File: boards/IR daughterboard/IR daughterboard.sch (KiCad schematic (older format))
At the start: 1 part, among them P0 HEADER

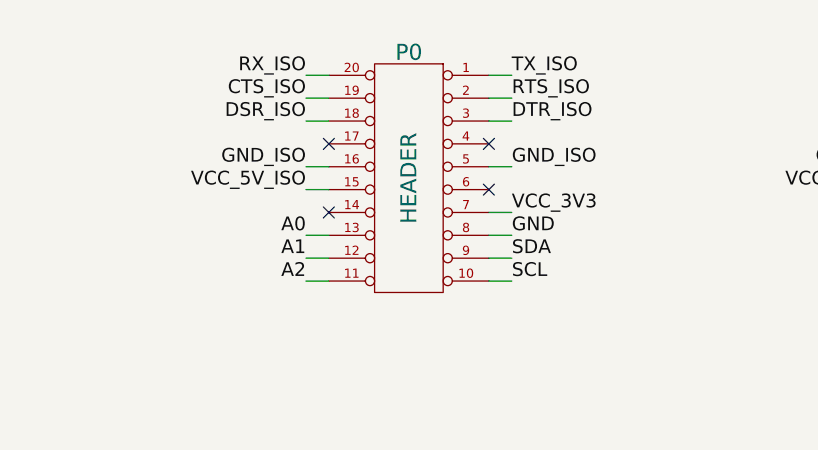
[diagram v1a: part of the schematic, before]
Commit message: Updated daughterboard header pinout in all sheets to be PMOD UART 4/4A compatible
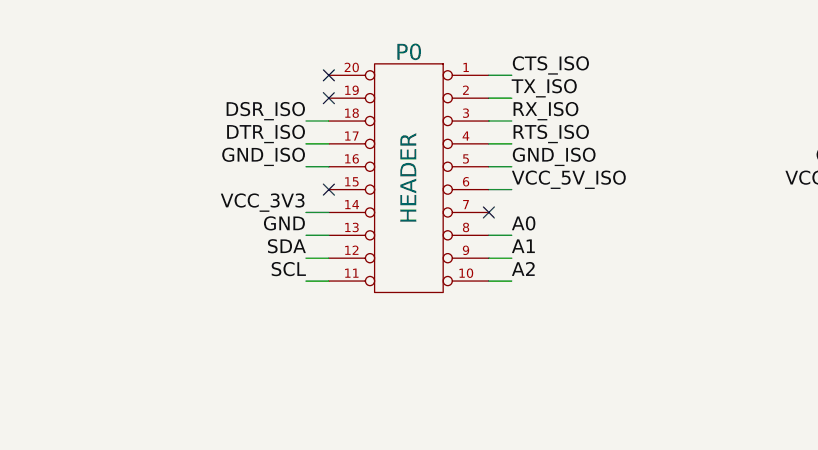
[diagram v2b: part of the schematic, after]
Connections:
- net A0: now also P0.8 (P8); no longer P0.13 (P13)
- net A1: now also P0.9 (P9); no longer P0.12 (P12)
- net A2: now also P0.10 (P10); no longer P0.11 (P11)
- net CTS_ISO: now also P0.1 (P1); no longer P0.19 (P19)
- net DTR_ISO: now also P0.17 (P17); no longer P0.3 (P3)
- net GND: now also P0.13 (P13); no longer P0.8 (P8)
- net RTS_ISO: now also P0.4 (P4); no longer P0.2 (P2)
- net RX_ISO: now also P0.3 (P3); no longer P0.20 (P20)
- net SCL: now also P0.11 (P11); no longer P0.10 (P10)
- net SDA: now also P0.12 (P12); no longer P0.9 (P9)
- net TX_ISO: now also P0.2 (P2); no longer P0.1 (P1)
- net VCC_3V3: now also P0.14 (P14); no longer P0.7 (P7)
- net VCC_5V_ISO: now also P0.6 (P6); no longer P0.15 (P15)
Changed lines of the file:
@@
 Sheet 1 3
 Title ""
-Date "26 jun 2014"
+Date "1 jul 2014"
 Rev ""
 Comp ""
@@
 $EndSheet
 Wire Wire Line
-	3750 3250 3650 3250
-Wire Wire Line
-	3750 3350 3650 3350
-Wire Wire Line
 	3750 3450 3650 3450
 Wire Wire Line
-	3750 3650 3650 3650
+	3750 3550 3650 3550
 Wire Wire Line
-	3750 3750 3650 3750
+	4450 3650 4550 3650
 Wire Wire Line
-	3750 3950 3650 3950
+	4450 3750 4550 3750
+Wire Wire Line
+	4450 3950 4550 3950
 Wire Wire Line
 	4550 3250 4450 3250
@@
 	4550 3450 4450 3450
 Wire Wire Line
-	4550 3650 4450 3650
+	3650 3650 3750 3650
 Wire Wire Line
-	4550 3850 4450 3850
+	3650 3850 3750 3850
 Wire Wire Line
-	4550 3950 4450 3950
+	3650 3950 3750 3950
 Wire Wire Line
-	3750 4050 3650 4050
+	4450 4050 4550 4050
 Wire Wire Line
-	3750 4150 3650 4150
+	4450 4150 4550 4150
 Wire Wire Line
-	4550 4050 4450 4050
+	3650 4050 3750 4050
 Wire Wire Line
-	4550 4150 4450 4150
+	3650 4150 3750 4150
 Text Label 4550 3250 0    60   ~ 0
+CTS_ISO
+Text Label 4550 3350 0    60   ~ 0
 TX_ISO
-Text Label 4550 3350 0    60   ~ 0
-RTS_ISO
 Text Label 4550 3450 0    60   ~ 0
+RX_ISO
+Text Label 3650 3850 2    60   ~ 0
+VCC_3V3
+Text Label 3650 3950 2    60   ~ 0
+GND
+Text Label 3650 4050 2    60   ~ 0
+SDA
+Text Label 3650 4150 2    60   ~ 0
+SCL
+Text Label 4550 4150 0    60   ~ 0
+A2
+Text Label 4550 4050 0    60   ~ 0
+A1
+Text Label 4550 3950 0    60   ~ 0
+A0
+Text Label 4550 3750 0    60   ~ 0
+VCC_5V_ISO
+Text Label 4550 3650 0    60   ~ 0
+GND_ISO
+Text Label 3650 3550 2    60   ~ 0
 DTR_ISO
-Text Label 4550 3850 0    60   ~ 0
-VCC_3V3
-Text Label 4550 3950 0    60   ~ 0
-GND
-Text Label 4550 4050 0    60   ~ 0
-SDA
-Text Label 4550 4150 0    60   ~ 0
-SCL
-Text Label 3650 4150 2    60   ~ 0
-A2
-Text Label 3650 4050 2    60   ~ 0
-A1
-Text Label 3650 3950 2    60   ~ 0
-A0
-Text Label 3650 3750 2    60   ~ 0
-VCC_5V_ISO
+Text Label 3650 3450 2    60   ~ 0
+DSR_ISO
 Text Label 3650 3650 2    60   ~ 0
 GND_ISO
-Text Label 3650 3450 2    60   ~ 0
-DSR_ISO
-Text Label 3650 3350 2    60   ~ 0
-CTS_ISO
-Text Label 3650 3250 2    60   ~ 0
-RX_ISO
-Text Label 4550 3650 0    60   ~ 0
-GND_ISO
-NoConn ~ 4450 3750
-NoConn ~ 4450 3550
-NoConn ~ 3750 3550
-NoConn ~ 3750 3850
+NoConn ~ 4450 3850
+NoConn ~ 3750 3250
+NoConn ~ 3750 3750
 Wire Wire Line
 	6400 3250 6250 3250
@@
 Text Notes 950  7350 0    60   ~ 0
 This sheet abstracts the daughterboard circuits into a hierarchical sheet \nso that they can be integrated into serial expansion motherboard schematic (and PCB) if needed
+Wire Wire Line
+	4450 3550 4550 3550
+Text Label 4550 3550 0    60   ~ 0
+RTS_ISO
+NoConn ~ 3750 3350
 $EndSCHEMATC

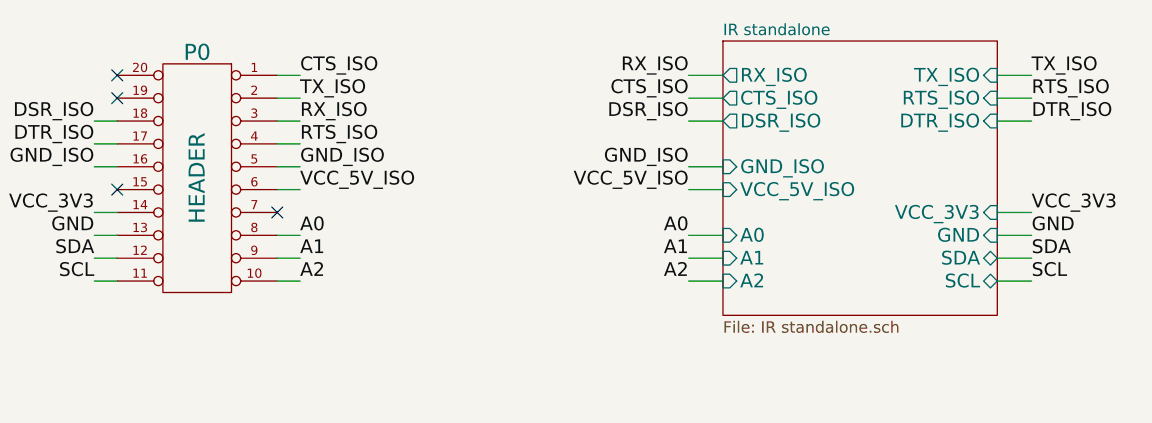
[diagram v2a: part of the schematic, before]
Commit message: Updated IR dboard to use RS232 adapter block; Changed power hierarchy pins in RS232 adapter block and GPIO 8 sheet as passive type
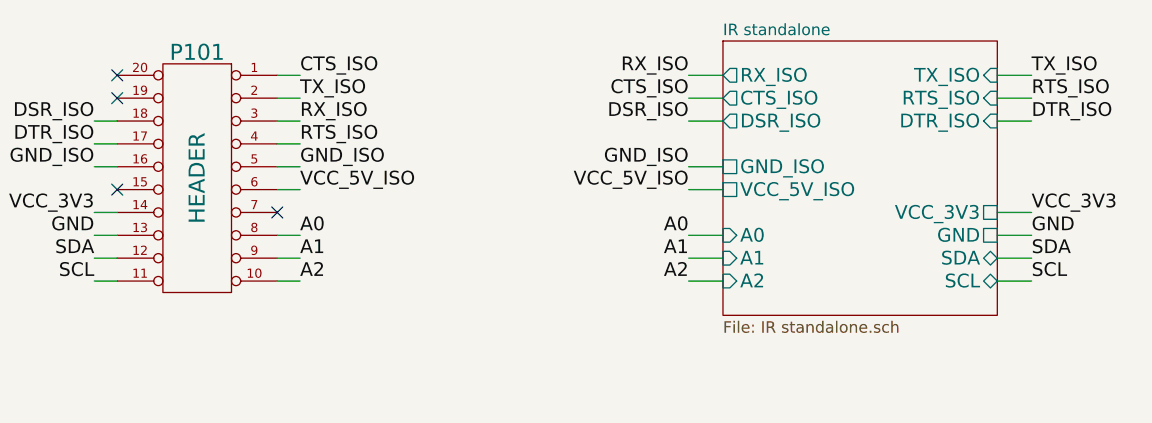
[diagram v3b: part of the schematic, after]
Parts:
- renumbered P0 to P101
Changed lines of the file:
@@
 LIBS:csmall
 LIBS:ISL83387E
+LIBS:pic16f1704
 LIBS:IR daughterboard-cache
 EELAYER 27 0
@@
 $Descr A4 11693 8268
 encoding utf-8
-Sheet 1 3
+Sheet 1 4
 Title ""
 Date "1 jul 2014"
@@
 $EndDescr
 $Comp
-L DIL20 P0
+L DIL20 P101
 U 1 1 53AB69C0
 P 4100 3700
-F 0 "P0" H 4100 4250 70  0000 C CNN
+F 0 "P101" H 4100 4250 70  0000 C CNN
 F 1 "HEADER" V 4100 3700 70  0000 C CNN
 F 2 "" H 4100 3700 60  0000 C CNN
@@
 F6 "DTR_ISO" I R 7600 3450 60
 F7 "DSR_ISO" O L 6400 3450 60
-F8 "VCC_3V3" I R 7600 3850 60
-F9 "GND" I R 7600 3950 60
-F10 "VCC_5V_ISO" I L 6400 3750 60
-F11 "GND_ISO" I L 6400 3650 60
+F8 "VCC_3V3" U R 7600 3850 60
+F9 "GND" U R 7600 3950 60
+F10 "VCC_5V_ISO" U L 6400 3750 60
+F11 "GND_ISO" U L 6400 3650 60
 F12 "SDA" B R 7600 4050 60
 F13 "SCL" B R 7600 4150 60

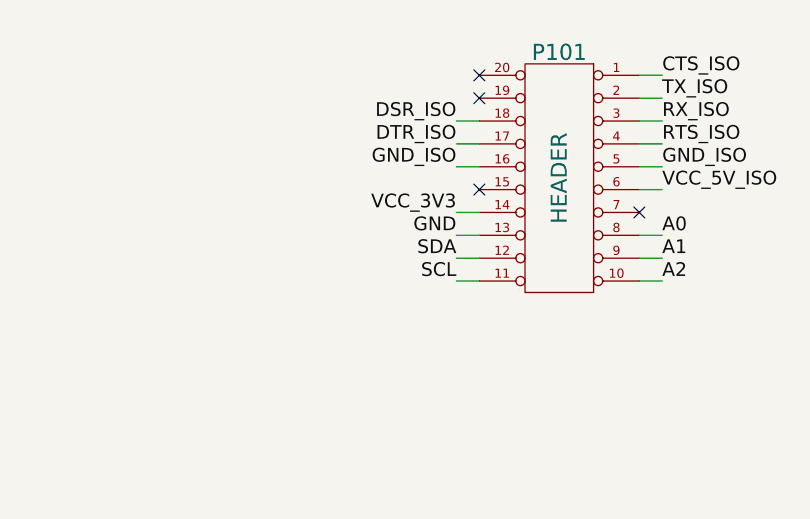
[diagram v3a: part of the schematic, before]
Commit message: Rearranged EEPROM pins in dboard slot pinout to be compatible with PMOD I2C interface
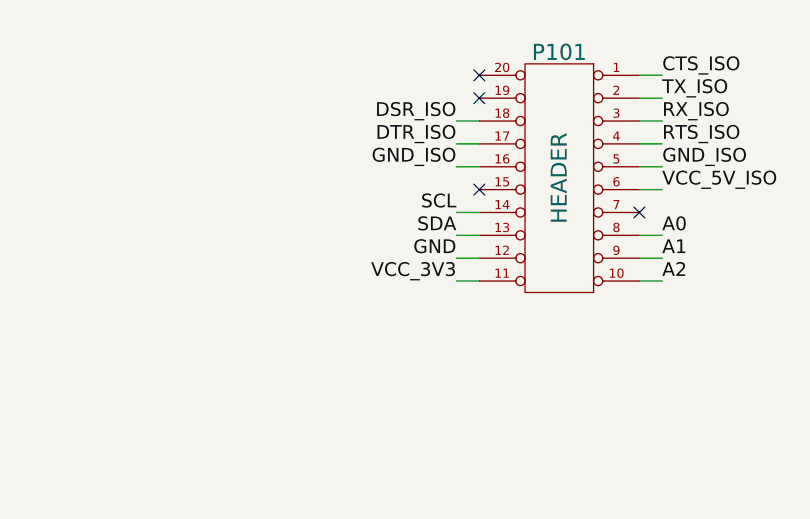
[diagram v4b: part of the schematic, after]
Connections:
- net GND: now also P101.12 (P12); no longer P101.13 (P13)
- net SCL: now also P101.14 (P14); no longer P101.11 (P11)
- net SDA: now also P101.13 (P13); no longer P101.12 (P12)
- net VCC_3V3: now also P101.11 (P11); no longer P101.14 (P14)
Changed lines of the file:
@@
 Sheet 1 4
 Title ""
-Date "1 jul 2014"
+Date "2 jul 2014"
 Rev ""
 Comp ""
@@
 	3650 3650 3750 3650
 Wire Wire Line
-	3650 3850 3750 3850
+	3650 4150 3750 4150
 Wire Wire Line
-	3650 3950 3750 3950
+	3650 4050 3750 4050
 Wire Wire Line
 	4450 4050 4550 4050
@@
 	4450 4150 4550 4150
 Wire Wire Line
-	3650 4050 3750 4050
+	3650 3950 3750 3950
 Wire Wire Line
-	3650 4150 3750 4150
+	3650 3850 3750 3850
 Text Label 4550 3250 0    60   ~ 0
 CTS_ISO
@@
 Text Label 4550 3450 0    60   ~ 0
 RX_ISO
+Text Label 3650 4150 2    60   ~ 0
+VCC_3V3
+Text Label 3650 4050 2    60   ~ 0
+GND
+Text Label 3650 3950 2    60   ~ 0
+SDA
 Text Label 3650 3850 2    60   ~ 0
-VCC_3V3
-Text Label 3650 3950 2    60   ~ 0
-GND
-Text Label 3650 4050 2    60   ~ 0
-SDA
-Text Label 3650 4150 2    60   ~ 0
 SCL
 Text Label 4550 4150 0    60   ~ 0

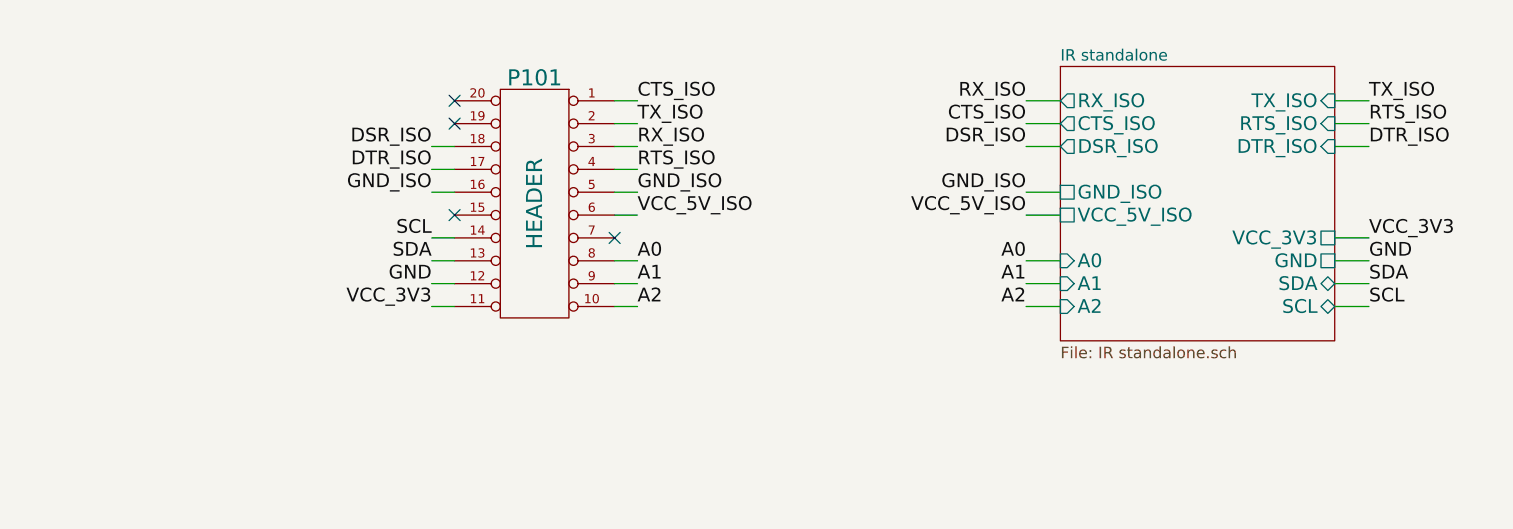
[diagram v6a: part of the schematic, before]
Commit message: Updated IR dboard to use new dboard_slot component
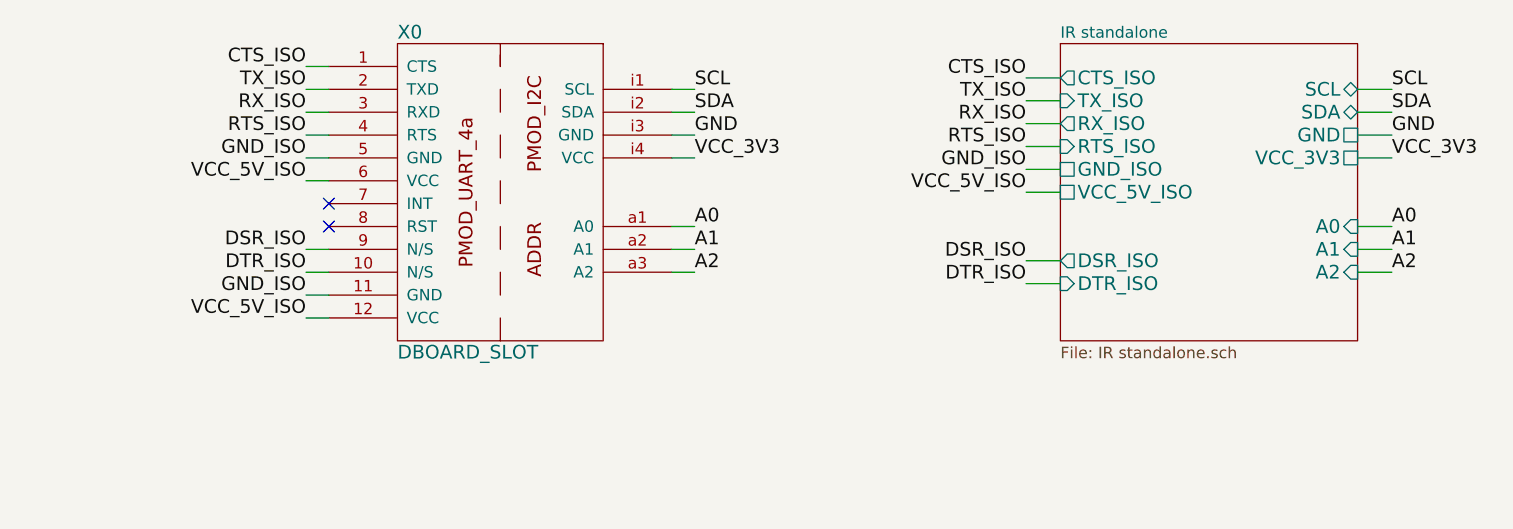
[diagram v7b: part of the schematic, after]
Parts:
- removed P101: HEADER, symbol DIL20
- added X0: DBOARD_SLOT, ~, symbol DBOARD_SLOT
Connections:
- net A0: now also X0.a1 (A0)
- net A1: now also X0.a2 (A1)
- net A2: now also X0.a3 (A2)
- net CTS_ISO: now also X0.1 (CTS)
- net DSR_ISO: now also X0.9 (N/S)
- net DTR_ISO: now also X0.10 (N/S)
- net GND: now also X0.i3 (GND)
- net GND_ISO: now also X0.11 (GND), X0.5 (GND)
- net RTS_ISO: now also X0.4 (RTS)
- net RX_ISO: now also X0.3 (RXD)
- net SCL: now also X0.i1 (SCL)
- net SDA: now also X0.i2 (SDA)
- net TX_ISO: now also X0.2 (TXD)
- net VCC_3V3: now also X0.i4 (VCC)
- net VCC_5V_ISO: now also X0.12 (VCC), X0.6 (VCC)
- no-connect marks 4 -> 2
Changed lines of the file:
@@
 LIBS:pic16f1704
 LIBS:switchcraft_35rasmt2bhntrx
+LIBS:dboard_slot
+LIBS:RS232C daughterboard-cache
 LIBS:IR daughterboard-cache
 EELAYER 27 0
@@
 Comment4 ""
 $EndDescr
+Wire Wire Line
+	3200 3900 3100 3900
+Wire Wire Line
+	3200 4000 3100 4000
+Wire Wire Line
+	4700 3800 4800 3800
+Wire Wire Line
+	3100 4100 3200 4100
+Wire Wire Line
+	4800 3500 4700 3500
+Wire Wire Line
+	4800 3400 4700 3400
+Wire Wire Line
+	4700 3900 4800 3900
+Wire Wire Line
+	4700 4000 4800 4000
+Wire Wire Line
+	4800 3300 4700 3300
+Wire Wire Line
+	4800 3200 4700 3200
+Text Label 4800 3500 0    60   ~ 0
+VCC_3V3
+Text Label 4800 3400 0    60   ~ 0
+GND
+Text Label 4800 3300 0    60   ~ 0
+SDA
+Text Label 4800 3200 0    60   ~ 0
+SCL
+Text Label 4800 4000 0    60   ~ 0
+A2
+Text Label 4800 3900 0    60   ~ 0
+A1
+Text Label 4800 3800 0    60   ~ 0
+A0
+Text Label 3100 4000 2    60   ~ 0
+DTR_ISO
+Text Label 3100 3900 2    60   ~ 0
+DSR_ISO
+Text Label 3100 4100 2    60   ~ 0
+GND_ISO
+Wire Wire Line
+	6400 3350 6250 3350
+Text Label 6250 3350 2    60   ~ 0
+RX_ISO
+Wire Wire Line
+	6400 3150 6250 3150
+Text Label 6250 3150 2    60   ~ 0
+CTS_ISO
+Wire Wire Line
+	6400 3950 6250 3950
+Text Label 6250 3950 2    60   ~ 0
+DSR_ISO
+Wire Wire Line
+	6250 3250 6400 3250
+Text Label 6250 3250 2    60   ~ 0
+TX_ISO
+Wire Wire Line
+	6250 3450 6400 3450
+Wire Wire Line
+	6250 4050 6400 4050
+Text Label 6250 3450 2    60   ~ 0
+RTS_ISO
+Text Label 6250 4050 2    60   ~ 0
+DTR_ISO
+Wire Wire Line
+	6400 3650 6250 3650
+Text Label 6250 3650 2    60   ~ 0
+VCC_5V_ISO
+Wire Wire Line
+	6400 3550 6250 3550
+Text Label 6250 3550 2    60   ~ 0
+GND_ISO
+Wire Wire Line
+	7700 3800 7850 3800
+Wire Wire Line
+	7700 3900 7850 3900
+Wire Wire Line
+	7700 4000 7850 4000
+Text Label 7850 4000 0    60   ~ 0
+A2
+Text Label 7850 3900 0    60   ~ 0
+A1
+Text Label 7850 3800 0    60   ~ 0
+A0
+Wire Wire Line
+	7850 3300 7700 3300
+Wire Wire Line
+	7850 3200 7700 3200
+Text Label 7850 3300 0    60   ~ 0
+SDA
+Text Label 7850 3200 0    60   ~ 0
+SCL
+Wire Wire Line
+	7850 3400 7700 3400
+Text Label 7850 3500 0    60   ~ 0
+VCC_3V3
+Text Label 7850 3400 0    60   ~ 0
+GND
+Wire Wire Line
+	7700 3500 7850 3500
+Text Notes 950  7350 0    60   ~ 0
+This sheet abstracts the daughterboard circuits into a hierarchical sheet \nso that they can be integrated into serial expansion motherboard schematic (and PCB) if needed
 $Comp
-L DIL20 P101
-U 1 1 53AB69C0
-P 4100 3700
-F 0 "P101" H 4100 4250 70  0000 C CNN
-F 1 "HEADER" V 4100 3700 70  0000 C CNN
-F 2 "" H 4100 3700 60  0000 C CNN
-F 3 "" H 4100 3700 60  0000 C CNN
-	1    4100 3700
-	-1   0    0    -1
+L DBOARD_SLOT X0
+U 1 1 53B7E555
+P 3950 3650
+F 0 "X0" H 3500 4350 60  0000 L CNN
+F 1 "DBOARD_SLOT" H 3500 2950 60  0000 L CNN
+F 2 "~" H 4200 3750 60  0000 C CNN
+F 3 "~" H 4200 3750 60  0000 C CNN
+	1    3950 3650
+	1    0    0    -1
 $EndComp
+Wire Wire Line
+	3200 3500 3100 3500
+Wire Wire Line
+	3200 3600 3100 3600
+Wire Wire Line
+	3100 3100 3200 3100
+Wire Wire Line
+	3100 3200 3200 3200
+Wire Wire Line
+	3100 3300 3200 3300
+Text Label 3100 3100 2    60   ~ 0
+CTS_ISO
+Text Label 3100 3200 2    60   ~ 0
+TX_ISO
+Text Label 3100 3300 2    60   ~ 0
+RX_ISO
+Text Label 3100 3600 2    60   ~ 0
+VCC_5V_ISO
+Text Label 3100 3500 2    60   ~ 0
+GND_ISO
+Wire Wire Line
+	3200 3400 3100 3400
+Text Label 3100 3400 2    60   ~ 0
+RTS_ISO
+Wire Wire Line
+	3200 4200 3100 4200
+Text Label 3100 4200 2    60   ~ 0
+VCC_5V_ISO
+NoConn ~ 3200 3700
+NoConn ~ 3200 3800
 $Sheet
-S 6400 3100 1200 1200
+S 6400 3000 1300 1300
 U 53AB69CE
 F0 "IR standalone" 50
 F1 "IR standalone.sch" 50
-F2 "TX_ISO" I R 7600 3250 60
-F3 "RX_ISO" O L 6400 3250 60
-F4 "RTS_ISO" I R 7600 3350 60
-F5 "CTS_ISO" O L 6400 3350 60
-F6 "DTR_ISO" I R 7600 3450 60
-F7 "DSR_ISO" O L 6400 3450 60
-F8 "VCC_3V3" U R 7600 3850 60
-F9 "GND" U R 7600 3950 60
-F10 "VCC_5V_ISO" U L 6400 3750 60
-F11 "GND_ISO" U L 6400 3650 60
-F12 "SDA" B R 7600 4050 60
-F13 "SCL" B R 7600 4150 60
-F14 "A0" I L 6400 3950 60
-F15 "A1" I L 6400 4050 60
-F16 "A2" I L 6400 4150 60
+F2 "TX_ISO" I L 6400 3250 60
+F3 "RX_ISO" O L 6400 3350 60
+F4 "RTS_ISO" I L 6400 3450 60
+F5 "CTS_ISO" O L 6400 3150 60
+F6 "DTR_ISO" I L 6400 4050 60
+F7 "DSR_ISO" O L 6400 3950 60
+F8 "VCC_3V3" U R 7700 3500 60
+F9 "GND" U R 7700 3400 60
+F10 "VCC_5V_ISO" U L 6400 3650 60
+F11 "GND_ISO" U L 6400 3550 60
+F12 "SDA" B R 7700 3300 60
+F13 "SCL" B R 7700 3200 60
+F14 "A0" I R 7700 3800 60
+F15 "A1" I R 7700 3900 60
+F16 "A2" I R 7700 4000 60
 $EndSheet
-Wire Wire Line
-	3750 3450 3650 3450
-Wire Wire Line
-	3750 3550 3650 3550
-Wire Wire Line
-	4450 3650 4550 3650
-Wire Wire Line
-	4450 3750 4550 3750
-Wire Wire Line
-	4450 3950 4550 3950
-Wire Wire Line
-	4550 3250 4450 3250
-Wire Wire Line
-	4550 3350 4450 3350
-Wire Wire Line
-	4550 3450 4450 3450
-Wire Wire Line
-	3650 3650 3750 3650
-Wire Wire Line
-	3650 4150 3750 4150
-Wire Wire Line
-	3650 4050 3750 4050
-Wire Wire Line
-	4450 4050 4550 4050
-Wire Wire Line
-	4450 4150 4550 4150
-Wire Wire Line
-	3650 3950 3750 3950
-Wire Wire Line
-	3650 3850 3750 3850
-Text Label 4550 3250 0    60   ~ 0
-CTS_ISO
-Text Label 4550 3350 0    60   ~ 0
-TX_ISO
-Text Label 4550 3450 0    60   ~ 0
-RX_ISO
-Text Label 3650 4150 2    60   ~ 0
-VCC_3V3
-Text Label 3650 4050 2    60   ~ 0
-GND
-Text Label 3650 3950 2    60   ~ 0
-SDA
-Text Label 3650 3850 2    60   ~ 0
-SCL
-Text Label 4550 4150 0    60   ~ 0
-A2
-Text Label 4550 4050 0    60   ~ 0
-A1
-Text Label 4550 3950 0    60   ~ 0
-A0
-Text Label 4550 3750 0    60   ~ 0
-VCC_5V_ISO
-Text Label 4550 3650 0    60   ~ 0
-GND_ISO
-Text Label 3650 3550 2    60   ~ 0
-DTR_ISO
-Text Label 3650 3450 2    60   ~ 0
-DSR_ISO
-Text Label 3650 3650 2    60   ~ 0
-GND_ISO
-NoConn ~ 4450 3850
-NoConn ~ 3750 3250
-NoConn ~ 3750 3750
-Wire Wire Line
-	6400 3250 6250 3250
-Text Label 6250 3250 2    60   ~ 0
-RX_ISO
-Wire Wire Line
-	6400 3350 6250 3350
-Text Label 6250 3350 2    60   ~ 0
-CTS_ISO
-Wire Wire Line
-	6400 3450 6250 3450
-Text Label 6250 3450 2    60   ~ 0
-DSR_ISO
-Wire Wire Line
-	7750 3250 7600 3250
-Text Label 7750 3250 0    60   ~ 0
-TX_ISO
-Wire Wire Line
-	7750 3350 7600 3350
-Wire Wire Line
-	7750 3450 7600 3450
-Text Label 7750 3350 0    60   ~ 0
-RTS_ISO
-Text Label 7750 3450 0    60   ~ 0
-DTR_ISO
-Wire Wire Line
-	6400 3750 6250 3750
-Text Label 6250 3750 2    60   ~ 0
-VCC_5V_ISO
-Wire Wire Line
-	6400 3650 6250 3650
-Text Label 6250 3650 2    60   ~ 0
-GND_ISO
-Wire Wire Line
-	6400 3950 6250 3950
-Wire Wire Line
-	6400 4050 6250 4050
-Wire Wire Line
-	6400 4150 6250 4150
-Text Label 6250 4150 2    60   ~ 0
-A2
-Text Label 6250 4050 2    60   ~ 0
-A1
-Text Label 6250 3950 2    60   ~ 0
-A0
-Wire Wire Line
-	7750 4050 7600 4050
-Wire Wire Line
-	7750 4150 7600 4150
-Text Label 7750 4050 0    60   ~ 0
-SDA
-Text Label 7750 4150 0    60   ~ 0
-SCL
-Wire Wire Line
-	7750 3950 7600 3950
-Text Label 7750 3850 0    60   ~ 0
-VCC_3V3
-Text Label 7750 3950 0    60   ~ 0
-GND
-Wire Wire Line
-	7600 3850 7750 3850
-Text Notes 950  7350 0    60   ~ 0
-This sheet abstracts the daughterboard circuits into a hierarchical sheet \nso that they can be integrated into serial expansion motherboard schematic (and PCB) if needed
-Wire Wire Line
-	4450 3550 4550 3550
-Text Label 4550 3550 0    60   ~ 0
-RTS_ISO
-NoConn ~ 3750 3350
 $EndSCHEMATC
